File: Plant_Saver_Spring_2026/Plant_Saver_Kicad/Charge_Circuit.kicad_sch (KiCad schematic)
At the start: 23 parts, among them J1 1.25mm, Q1 G09P02L, Q12 G09P02L, Q2 G09P02L, Q3 G09P02L, Q4 ISP12DP06NMXTSA1, Q5 G09P02L, Q8 G09P02L, Q9 G09P02L, SW6 SA72SB0, U10 DW03C, U11 CDBA140SL-HF, U15 CDBA140SL-HF

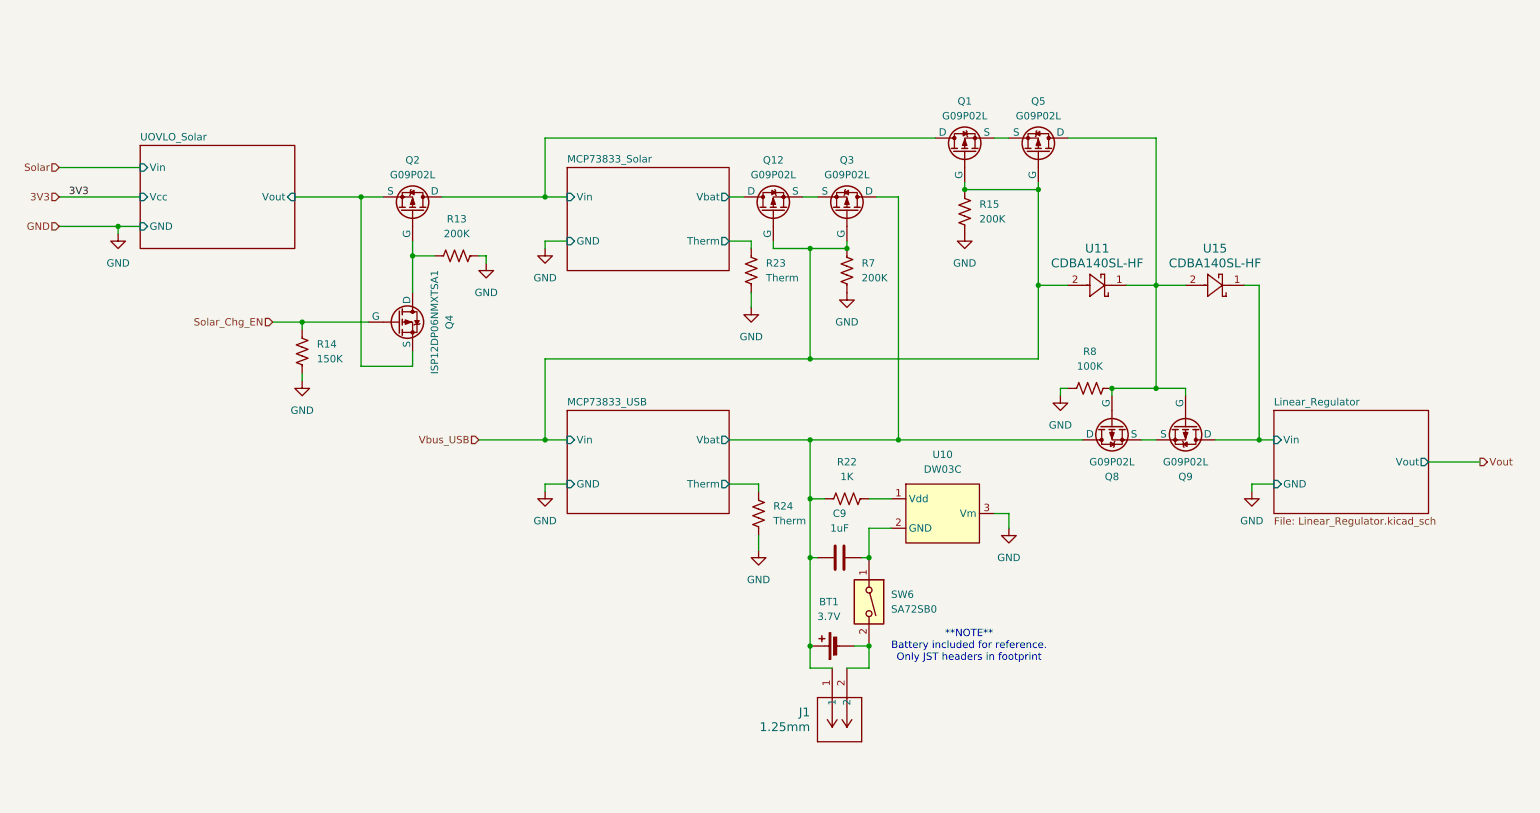
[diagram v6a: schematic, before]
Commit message: Footprint correction
Changed the DHT20 from a header pin to the recommended SIP. Also had to reannotate in order to assign footprints.
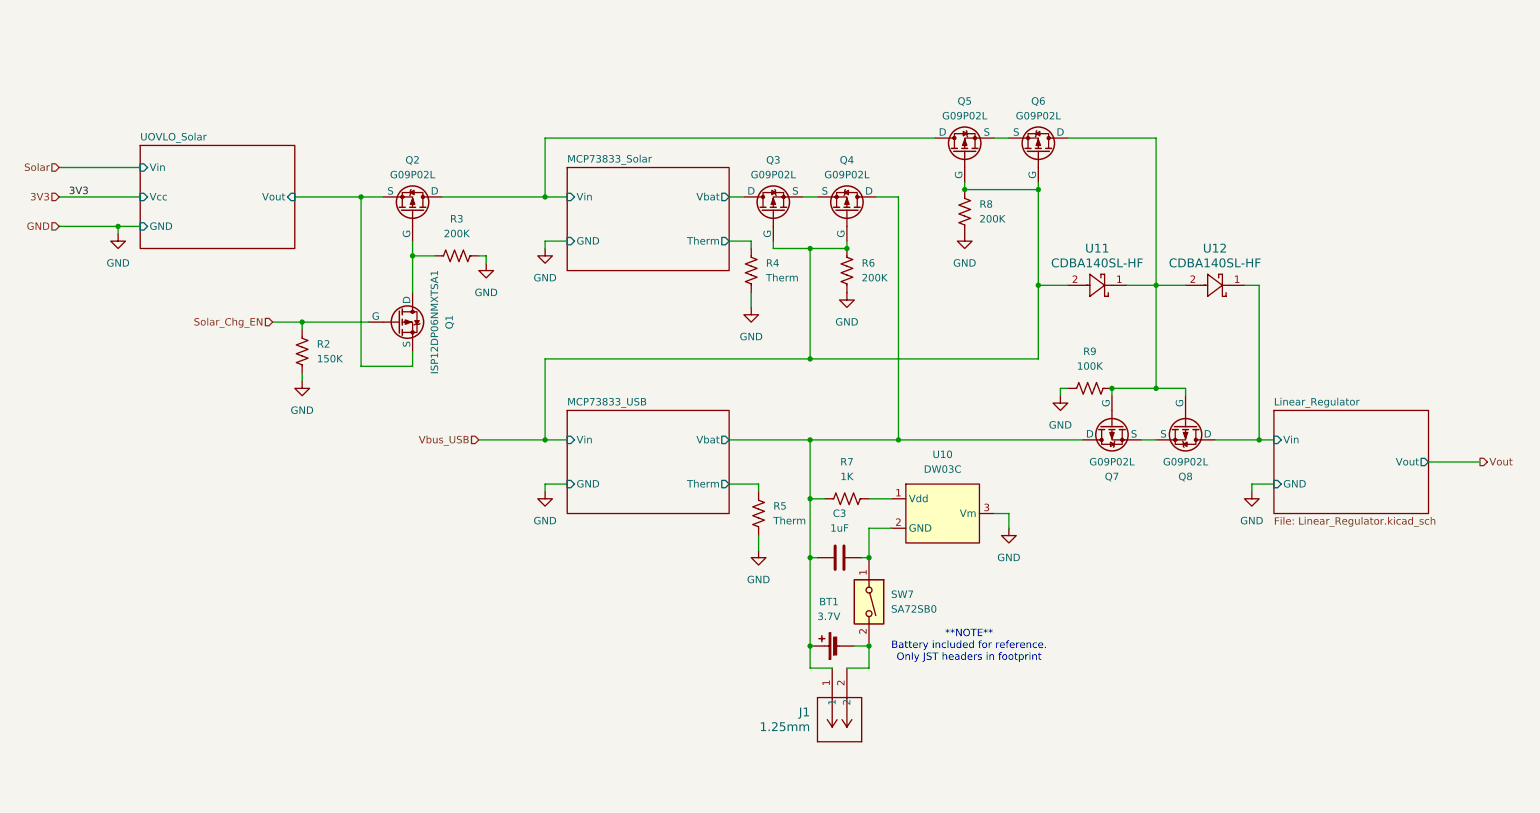
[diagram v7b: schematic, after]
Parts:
- U11: footprint CDBA-HF -> (none)
- U12: renamed from U15; footprint CDBA-HF -> (none)
- renumbered C9 to C3, Q4 to Q1, Q12 to Q3, Q3 to Q4, Q1 to Q5, Q5 to Q6, Q8 to Q7, Q9 to Q8, R14 to R2, R13 to R3, R23 to R4, R24 to R5, R7 to R6, R22 to R7, R15 to R8, R8 to R9, SW6 to SW7
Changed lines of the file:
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@@
 		(dnp no)
 		(fields_autoplaced yes)
-		(property "Reference" "R15"
+		(property "Reference" "R8"
 			(at 186.69 60.9599 0)
 			(effects
@@
 			(project "Plant_Saver_Dev"
 				(path "/7f244634-d37a-4ff0-ba36-8027330ab1bd/c1b5c94f-5fb5-4e2b-895b-5d171c372d7d"
-					(reference "R15")
+					(reference "R8")
 					(unit 1)
 				)
@@
 		(dnp no)
 		(fields_autoplaced yes)
-		(property "Reference" "R7"
+		(property "Reference" "R6"
 			(at 166.37 71.1199 0)
 			(effects
@@
 			(project "Plant_Saver_Dev"
 				(path "/7f244634-d37a-4ff0-ba36-8027330ab1bd/c1b5c94f-5fb5-4e2b-895b-5d171c372d7d"
-					(reference "R7")
+					(reference "R6")
 					(unit 1)
 				)
@@
 		(on_board yes)
 		(dnp no)
-		(property "Reference" "Q8"
+		(property "Reference" "Q7"
 			(at 209.55 107.95 90)
 			(effects
@@
 			(project "Plant_Saver_Kicad"
 				(path "/7f244634-d37a-4ff0-ba36-8027330ab1bd/c1b5c94f-5fb5-4e2b-895b-5d171c372d7d"
-					(reference "Q8")
+					(reference "Q7")
 					(unit 1)
 				)
@@
 		(on_board yes)
 		(dnp no)
-		(property "Reference" "Q1"
+		(property "Reference" "Q5"
 			(at 184.15 43.18 90)
 			(effects
@@
 			(project "Plant_Saver_Kicad"
 				(path "/7f244634-d37a-4ff0-ba36-8027330ab1bd/c1b5c94f-5fb5-4e2b-895b-5d171c372d7d"
-					(reference "Q1")
+					(reference "Q5")
 					(unit 1)
 				)
@@
 		(dnp no)
 		(fields_autoplaced yes)
-		(property "Reference" "#PWR0102"
+		(property "Reference" "#PWR016"
 			(at 111.76 116.84 0)
 			(effects
@@
 			(project "Plant_Saver_Dev"
 				(path "/7f244634-d37a-4ff0-ba36-8027330ab1bd/c1b5c94f-5fb5-4e2b-895b-5d171c372d7d"
-					(reference "#PWR0102")
+					(reference "#PWR016")
 					(unit 1)
 				)
@@
 		(dnp no)
 		(fields_autoplaced yes)
-		(property "Reference" "U15"
+		(property "Reference" "U12"
 			(at 227.33 68.58 0)
 			(effects
@@
 			)
 		)
-		(property "Footprint" "CDBA-HF"
+		(property "Footprint" ""
 			(at 232.41 74.93 0)
 			(effects
@@
 			(project "Plant_Saver_Kicad"
 				(path "/7f244634-d37a-4ff0-ba36-8027330ab1bd/c1b5c94f-5fb5-4e2b-895b-5d171c372d7d"
-					(reference "U15")
+					(reference "U12")
 					(unit 1)
 				)
@@
 		(dnp no)
 		(fields_autoplaced yes)
-		(property "Reference" "R14"
+		(property "Reference" "R2"
 			(at 72.39 85.0899 0)
 			(effects
@@
 			(project "Plant_Saver_Dev"
 				(path "/7f244634-d37a-4ff0-ba36-8027330ab1bd/c1b5c94f-5fb5-4e2b-895b-5d171c372d7d"
-					(reference "R14")
+					(reference "R2")
 					(unit 1)
 				)
@@
 		(dnp no)
 		(fields_autoplaced yes)
-		(property "Reference" "R8"
+		(property "Reference" "R9"
 			(at 205.74 86.36 90)
 			(effects
@@
 			(project "Plant_Saver_Dev"
 				(path "/7f244634-d37a-4ff0-ba36-8027330ab1bd/c1b5c94f-5fb5-4e2b-895b-5d171c372d7d"
-					(reference "R8")
+					(reference "R9")
 					(unit 1)
 				)
@@
 		(dnp no)
 		(fields_autoplaced yes)
-		(property "Reference" "R22"
+		(property "Reference" "R7"
 			(at 163.83 105.41 90)
 			(effects
@@
 			(project "Plant_Saver_Kicad"
 				(path "/7f244634-d37a-4ff0-ba36-8027330ab1bd/c1b5c94f-5fb5-4e2b-895b-5d171c372d7d"
-					(reference "R22")
+					(reference "R7")
 					(unit 1)
 				)
@@
 		(on_board yes)
 		(dnp no)
-		(property "Reference" "#PWR0107"
+		(property "Reference" "#PWR017"
 			(at 147.32 85.09 0)
 			(effects
@@
 			(project "Plant_Saver_Kicad"
 				(path "/7f244634-d37a-4ff0-ba36-8027330ab1bd/c1b5c94f-5fb5-4e2b-895b-5d171c372d7d"
-					(reference "#PWR0107")
+					(reference "#PWR017")
 					(unit 1)
 				)
@@
 		(dnp no)
 		(fields_autoplaced yes)
-		(property "Reference" "#PWR013"
+		(property "Reference" "#PWR014"
 			(at 101.6 77.47 0)
 			(effects
@@
 			(project "Plant_Saver_Dev"
 				(path "/7f244634-d37a-4ff0-ba36-8027330ab1bd/c1b5c94f-5fb5-4e2b-895b-5d171c372d7d"
-					(reference "#PWR013")
+					(reference "#PWR014")
 					(unit 1)
 				)
@@
 		(dnp no)
 		(fields_autoplaced yes)
-		(property "Reference" "R23"
+		(property "Reference" "R4"
 			(at 149.86 71.1199 0)
 			(effects
@@
 			(project "Plant_Saver_Kicad"
 				(path "/7f244634-d37a-4ff0-ba36-8027330ab1bd/c1b5c94f-5fb5-4e2b-895b-5d171c372d7d"
-					(reference "R23")
+					(reference "R4")
 					(unit 1)
 				)
@@
 		(on_board yes)
 		(dnp no)
-		(property "Reference" "Q12"
+		(property "Reference" "Q3"
 			(at 151.13 53.34 90)
 			(effects
@@
 			(project "Plant_Saver_Kicad"
 				(path "/7f244634-d37a-4ff0-ba36-8027330ab1bd/c1b5c94f-5fb5-4e2b-895b-5d171c372d7d"
-					(reference "Q12")
+					(reference "Q3")
 					(unit 1)
 				)
@@
 		(dnp no)
 		(fields_autoplaced yes)
-		(property "Reference" "#PWR0103"
+		(property "Reference" "#PWR022"
 			(at 200.66 100.33 0)
 			(effects
@@
 			(project "Plant_Saver_Dev"
 				(path "/7f244634-d37a-4ff0-ba36-8027330ab1bd/c1b5c94f-5fb5-4e2b-895b-5d171c372d7d"
-					(reference "#PWR0103")
+					(reference "#PWR022")
 					(unit 1)
 				)
@@
 		(dnp no)
 		(fields_autoplaced yes)
-		(property "Reference" "#PWR0101"
+		(property "Reference" "#PWR019"
 			(at 163.83 82.55 0)
 			(effects
@@
 			(project "Plant_Saver_Dev"
 				(path "/7f244634-d37a-4ff0-ba36-8027330ab1bd/c1b5c94f-5fb5-4e2b-895b-5d171c372d7d"
-					(reference "#PWR0101")
+					(reference "#PWR019")
 					(unit 1)
 				)
@@
 		(on_board yes)
 		(dnp no)
-		(property "Reference" "#PWR014"
+		(property "Reference" "#PWR013"
 			(at 69.85 97.79 0)
 			(effects
@@
 			(project "Plant_Saver_Dev"
 				(path "/7f244634-d37a-4ff0-ba36-8027330ab1bd/c1b5c94f-5fb5-4e2b-895b-5d171c372d7d"
-					(reference "#PWR014")
+					(reference "#PWR013")
 					(unit 1)
 				)
@@
 		(dnp no)
 		(fields_autoplaced yes)
-		(property "Reference" "C9"
+		(property "Reference" "C3"
 			(at 162.56 114.3 90)
 			(effects
@@
 			(project "Plant_Saver_Kicad"
 				(path "/7f244634-d37a-4ff0-ba36-8027330ab1bd/c1b5c94f-5fb5-4e2b-895b-5d171c372d7d"
-					(reference "C9")
+					(reference "C3")
 					(unit 1)
 				)
@@
 		(dnp no)
 		(fields_autoplaced yes)
-		(property "Reference" "#PWR0106"
+		(property "Reference" "#PWR018"
 			(at 148.59 127 0)
 			(effects
@@
 			(project "Plant_Saver_Kicad"
 				(path "/7f244634-d37a-4ff0-ba36-8027330ab1bd/c1b5c94f-5fb5-4e2b-895b-5d171c372d7d"
-					(reference "#PWR0106")
+					(reference "#PWR018")
 					(unit 1)
 				)
@@
 			)
 		)
-		(property "Footprint" "CDBA-HF"
+		(property "Footprint" ""
 			(at 212.09 74.93 0)
 			(effects
@@
 		(on_board yes)
 		(dnp no)
-		(property "Reference" "#PWR0104"
+		(property "Reference" "#PWR023"
 			(at 233.68 116.84 0)
 			(effects
@@
 			(project "Plant_Saver_Dev"
 				(path "/7f244634-d37a-4ff0-ba36-8027330ab1bd/c1b5c94f-5fb5-4e2b-895b-5d171c372d7d"
-					(reference "#PWR0104")
+					(reference "#PWR023")
 					(unit 1)
 				)
@@
 		(on_board yes)
 		(dnp no)
-		(property "Reference" "Q3"
+		(property "Reference" "Q4"
 			(at 163.83 53.34 90)
 			(effects
@@
 			(project "Plant_Saver_Kicad"
 				(path "/7f244634-d37a-4ff0-ba36-8027330ab1bd/c1b5c94f-5fb5-4e2b-895b-5d171c372d7d"
-					(reference "Q3")
+					(reference "Q4")
 					(unit 1)
 				)
@@
 		(on_board yes)
 		(dnp no)
-		(property "Reference" "Q5"
+		(property "Reference" "Q6"
 			(at 196.85 43.18 90)
 			(effects
@@
 			(project "Plant_Saver_Kicad"
 				(path "/7f244634-d37a-4ff0-ba36-8027330ab1bd/c1b5c94f-5fb5-4e2b-895b-5d171c372d7d"
-					(reference "Q5")
+					(reference "Q6")
 					(unit 1)
 				)
@@
 		(dnp no)
 		(fields_autoplaced yes)
-		(property "Reference" "SW6"
+		(property "Reference" "SW7"
 			(at 171.45 128.2699 90)
 			(effects
@@
 			(project ""
 				(path "/7f244634-d37a-4ff0-ba36-8027330ab1bd/c1b5c94f-5fb5-4e2b-895b-5d171c372d7d"
-					(reference "SW6")
+					(reference "SW7")
 					(unit 1)
 				)
@@
 		(dnp no)
 		(fields_autoplaced yes)
-		(property "Reference" "R13"
+		(property "Reference" "R3"
 			(at 96.52 63.5 90)
 			(effects
@@
 			(project ""
 				(path "/7f244634-d37a-4ff0-ba36-8027330ab1bd/c1b5c94f-5fb5-4e2b-895b-5d171c372d7d"
-					(reference "R13")
+					(reference "R3")
 					(unit 1)
 				)
@@
 		(on_board yes)
 		(dnp no)
-		(property "Reference" "Q9"
+		(property "Reference" "Q8"
 			(at 222.25 107.95 90)
 			(effects
@@
 			(project "Plant_Saver_Kicad"
 				(path "/7f244634-d37a-4ff0-ba36-8027330ab1bd/c1b5c94f-5fb5-4e2b-895b-5d171c372d7d"
-					(reference "Q9")
+					(reference "Q8")
 					(unit 1)
 				)
@@
 		(dnp no)
 		(fields_autoplaced yes)
-		(property "Reference" "#PWR0105"
+		(property "Reference" "#PWR020"
 			(at 184.15 72.39 0)
 			(effects
@@
 			(project "Plant_Saver_Dev"
 				(path "/7f244634-d37a-4ff0-ba36-8027330ab1bd/c1b5c94f-5fb5-4e2b-895b-5d171c372d7d"
-					(reference "#PWR0105")
+					(reference "#PWR020")
 					(unit 1)
 				)
@@
 		(dnp no)
 		(fields_autoplaced yes)
-		(property "Reference" "#PWR03"
+		(property "Reference" "#PWR021"
 			(at 191.77 123.19 0)
 			(effects
@@
 			(project "Plant_Saver_Kicad"
 				(path "/7f244634-d37a-4ff0-ba36-8027330ab1bd/c1b5c94f-5fb5-4e2b-895b-5d171c372d7d"
-					(reference "#PWR03")
+					(reference "#PWR021")
 					(unit 1)
 				)
@@
 		(on_board yes)
 		(dnp no)
-		(property "Reference" "Q4"
+		(property "Reference" "Q1"
 			(at 95.25 81.28 90)
 			(effects
@@
 			(project "Plant_Saver_Dev"
 				(path "/7f244634-d37a-4ff0-ba36-8027330ab1bd/c1b5c94f-5fb5-4e2b-895b-5d171c372d7d"
-					(reference "Q4")
+					(reference "Q1")
 					(unit 1)
 				)
@@
 		(dnp no)
 		(fields_autoplaced yes)
-		(property "Reference" "R24"
+		(property "Reference" "R5"
 			(at 151.13 113.0299 0)
 			(effects
@@
 			(project "Plant_Saver_Kicad"
 				(path "/7f244634-d37a-4ff0-ba36-8027330ab1bd/c1b5c94f-5fb5-4e2b-895b-5d171c372d7d"
-					(reference "R24")
-					(unit 1)
-				)
+					(reference "R5")
+					(unit 1)
+				)

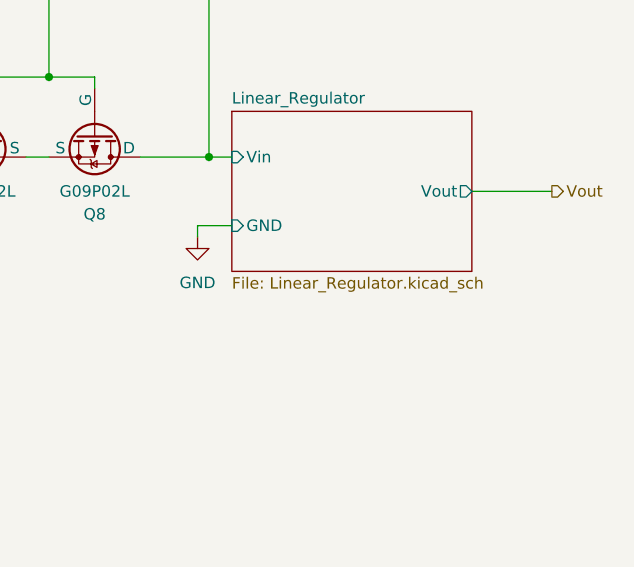
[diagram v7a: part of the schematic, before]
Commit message: Fixed USB-C and Linear Regulator Sheetfiles
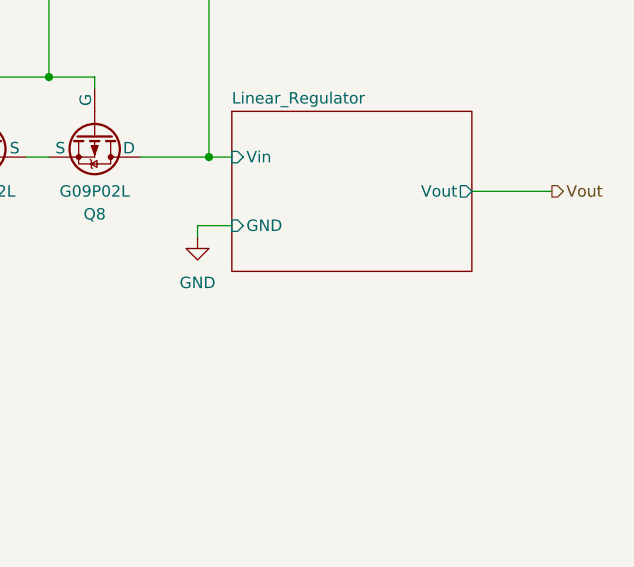
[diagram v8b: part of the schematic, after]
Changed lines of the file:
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@@
 				)
 				(justify left top)
+				(hide yes)
 			)
 		)
